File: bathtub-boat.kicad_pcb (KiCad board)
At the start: 2 copper layers, 61 x 35 mm, 61 parts, among them J1 I2C, J2 SPI, J3 I2C, J4 DS18B20, J5 1WireTRS, SW1 MODE, SW2 RESET, SW3 POWER, SW4 A, U1 esp-01m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

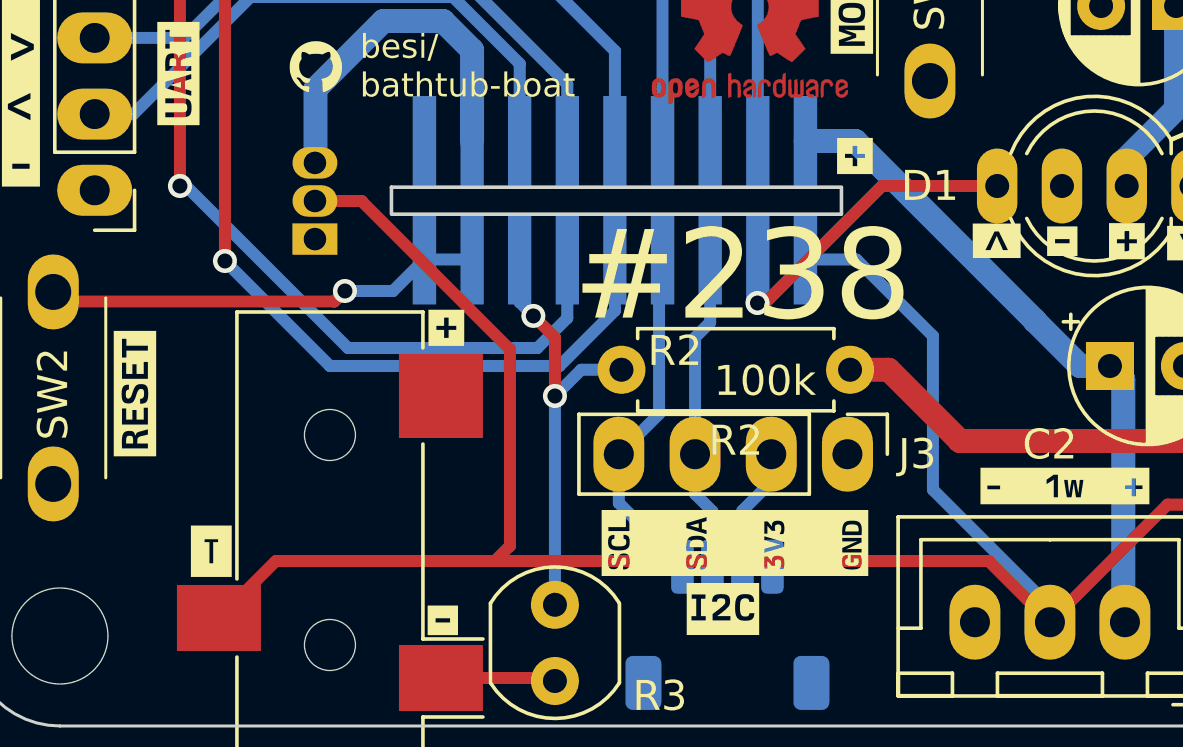
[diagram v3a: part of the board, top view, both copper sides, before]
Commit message: Add solder jumper and testpoint for IO16
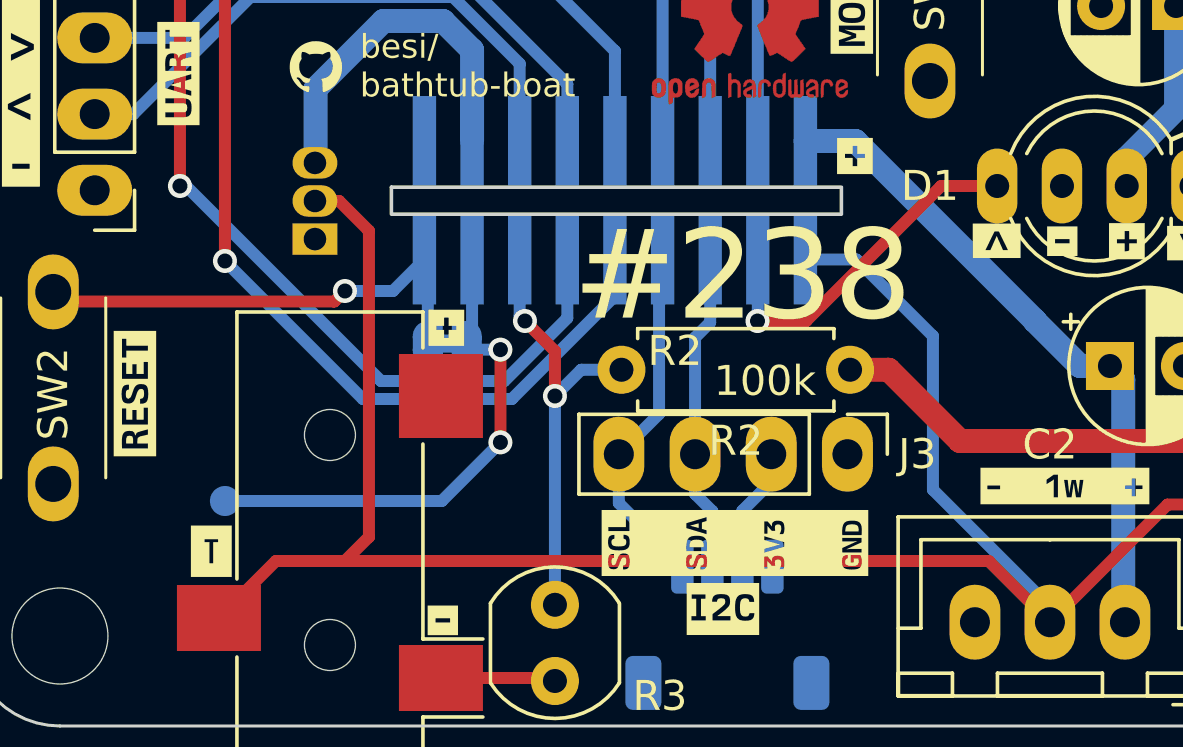
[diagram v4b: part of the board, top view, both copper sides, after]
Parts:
- added JP1: DS, Jumper:SolderJumper-2_P1.3mm_Bridged_RoundedPad1.0x1.5mm, B.Cu at (115.9, 87.3)
- added TP1: IO16, TestPoint:TestPoint_Pad_D1.0mm, B.Cu at (108.5, 92.5)
- moved kibuzzard-65B79508 3.68 mm to (126.5, 92.7)
- moved G*** 1.41 mm to (114.6, 92.6)
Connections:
- SW2 pad 2: Net-(U1-GP16) -> Net-(JP1-B)
- U1 pad 17: Net-(U1-GP16) -> Net-(JP1-A)
- U1 pad 18: Net-(U1-GP16) -> Net-(JP1-B)
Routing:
- net Net-(JP1-A): track 0.00 -> 17.2 mm, vias 0 -> 2
- net Net-(JP1-B): track 0.00 -> 15.1 mm, vias 0 -> 1
- net Net-(U1-GP16): track 14.7 -> 0.00 mm, vias 1 -> 0
- net Temp: track 70.7 -> 68.5 mm
- net SPI_CLK: track 48.6 -> 49.5 mm
- net Neopixel: track 11.1 -> 11.9 mm
- net SPI_MISO: track 37.1 -> 37.8 mm
